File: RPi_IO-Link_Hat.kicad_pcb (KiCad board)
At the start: 2 copper layers, 65 x 56 mm, 50 parts, among them J1 Jack-DC, J2 Raspberry_Pi_2_3, J3 Conn_01x03_Male, J4 Conn_01x03_Male, J5 Conn_01x03_Male, J6 Conn_01x03_Male, Q1 Q_PMOS_GSD, Q2 Q_NMOS_GSD, Q3 Q_NMOS_GSD, Q4 FQT7N10LTF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

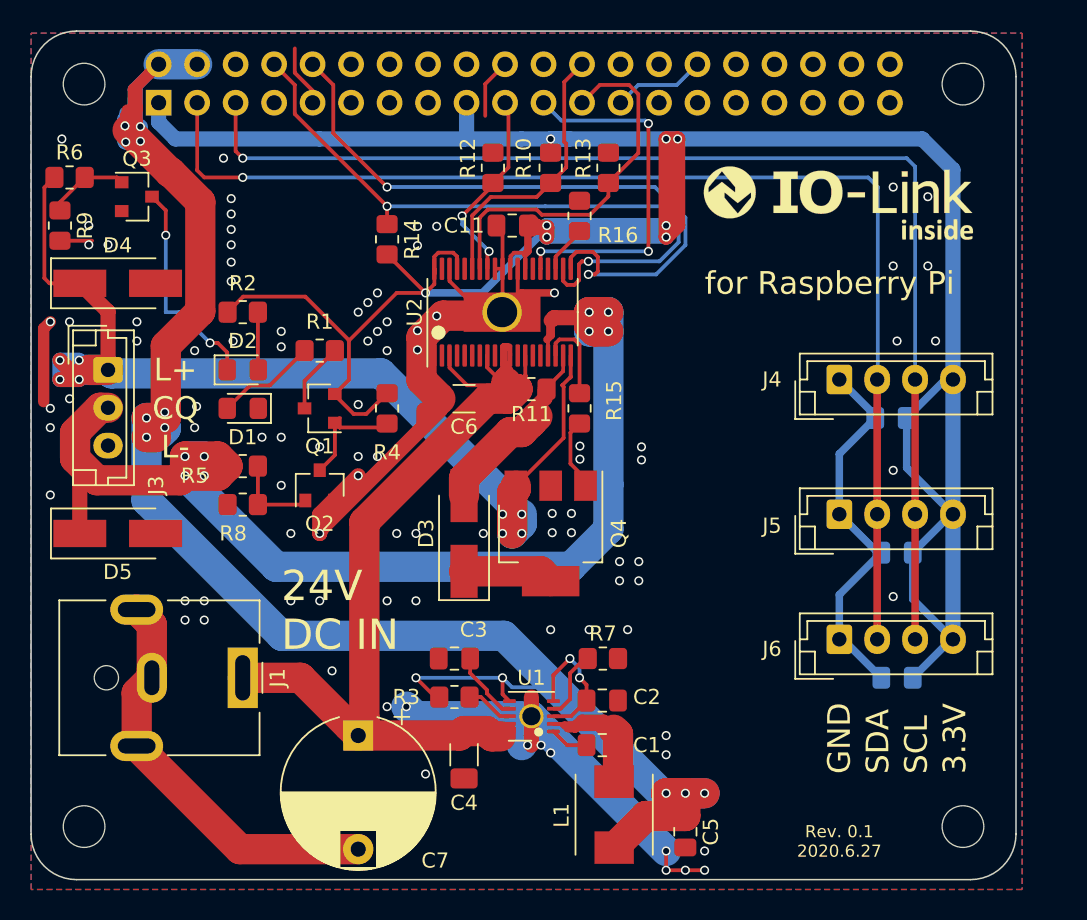
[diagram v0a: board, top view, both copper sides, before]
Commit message: fix: 改善 - CQ H で LED を点灯させるようにした - TP を追加
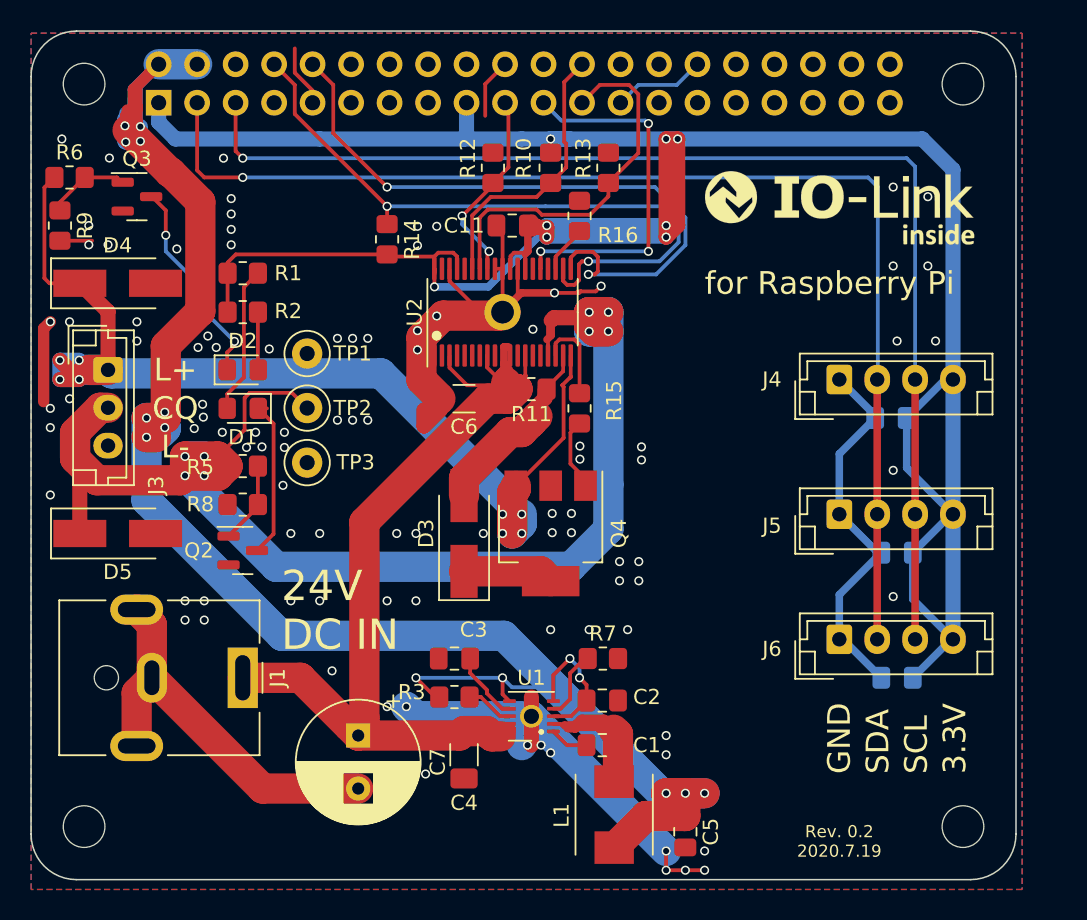
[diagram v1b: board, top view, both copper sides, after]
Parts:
- removed G0: LOGO, Local:io-link-logo-small
- removed Q1: Q_PMOS_GSD, Package_TO_SOT_SMD:SOT-23
- removed R4: 10k, Resistor_SMD:R_0805_2012Metric_Pad1.20x1.40mm_HandSolder
- added G***: LOGO, Local:io-link-logo-small, F.Cu at (71.2, 45.4)
- added TP1: TestPoint, TestPoint:TestPoint_Loop_D1.80mm_Drill1.0mm_Beaded, F.Cu at (36.0, 54.8)
- added TP2: TestPoint, TestPoint:TestPoint_Loop_D1.80mm_Drill1.0mm_Beaded, F.Cu at (36.0, 58.4)
- added TP3: TestPoint, TestPoint:TestPoint_Loop_D1.80mm_Drill1.0mm_Beaded, F.Cu at (36.0, 62.0)
- C7: footprint Capacitor_THT:CP_Radial_D10.0mm_P7.50mm -> Capacitor_THT:CP_Radial_D8.0mm_P3.50mm
- D1: value GREEN LED -> RED LED
- D2: value RED LED -> GREEN LED
- Q4: footprint Package_TO_SOT_SMD:SOT-223-3_TabPin2 -> Local:SOT-223-3_TabPin2_empty
- moved R1 7.21 mm to (31.8, 49.5), turned to 0 degrees
- moved Q2 6.66 mm to (31.8, 67.8), turned to 0 degrees
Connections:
- D1 pad 1: GND -> Net-(D1-Pad1)
- Q2 pad 3: Net-(Q1-Pad1) -> Net-(D1-Pad1)
- R1 pad 1: Net-(Q1-Pad3) -> +3V3
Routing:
- net +3V3: track 203.7 -> 187.5 mm
- net GND: track 155.3 -> 143.2 mm, vias 97 -> 98
- net Net-(D1-Pad1): track 0.00 -> 10.8 mm
- net CQ1: track 91.9 -> 101.2 mm
- net Net-(Q1-Pad1): track 8.12 -> 0.00 mm
- net Net-(Q1-Pad3): track 4.64 -> 0.00 mm
- net Net-(D1-Pad2): track 6.68 -> 9.76 mm
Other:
- board text added: "Rev. 0.2 2020.7.19"
- board text removed: "Rev. 0.1 2020.6.27"
